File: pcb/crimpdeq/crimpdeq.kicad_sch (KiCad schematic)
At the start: 47 parts, among them J2 USB4105-GF-A, Q1 SS8550, Q2 DMG3415U, U1 ESP32-C3-MINI-1, U2 MCP73831T-2ACI/OT, U3 HX711, U4 Rust_Board, U5 MAX17048G+T10, U6 SY8088

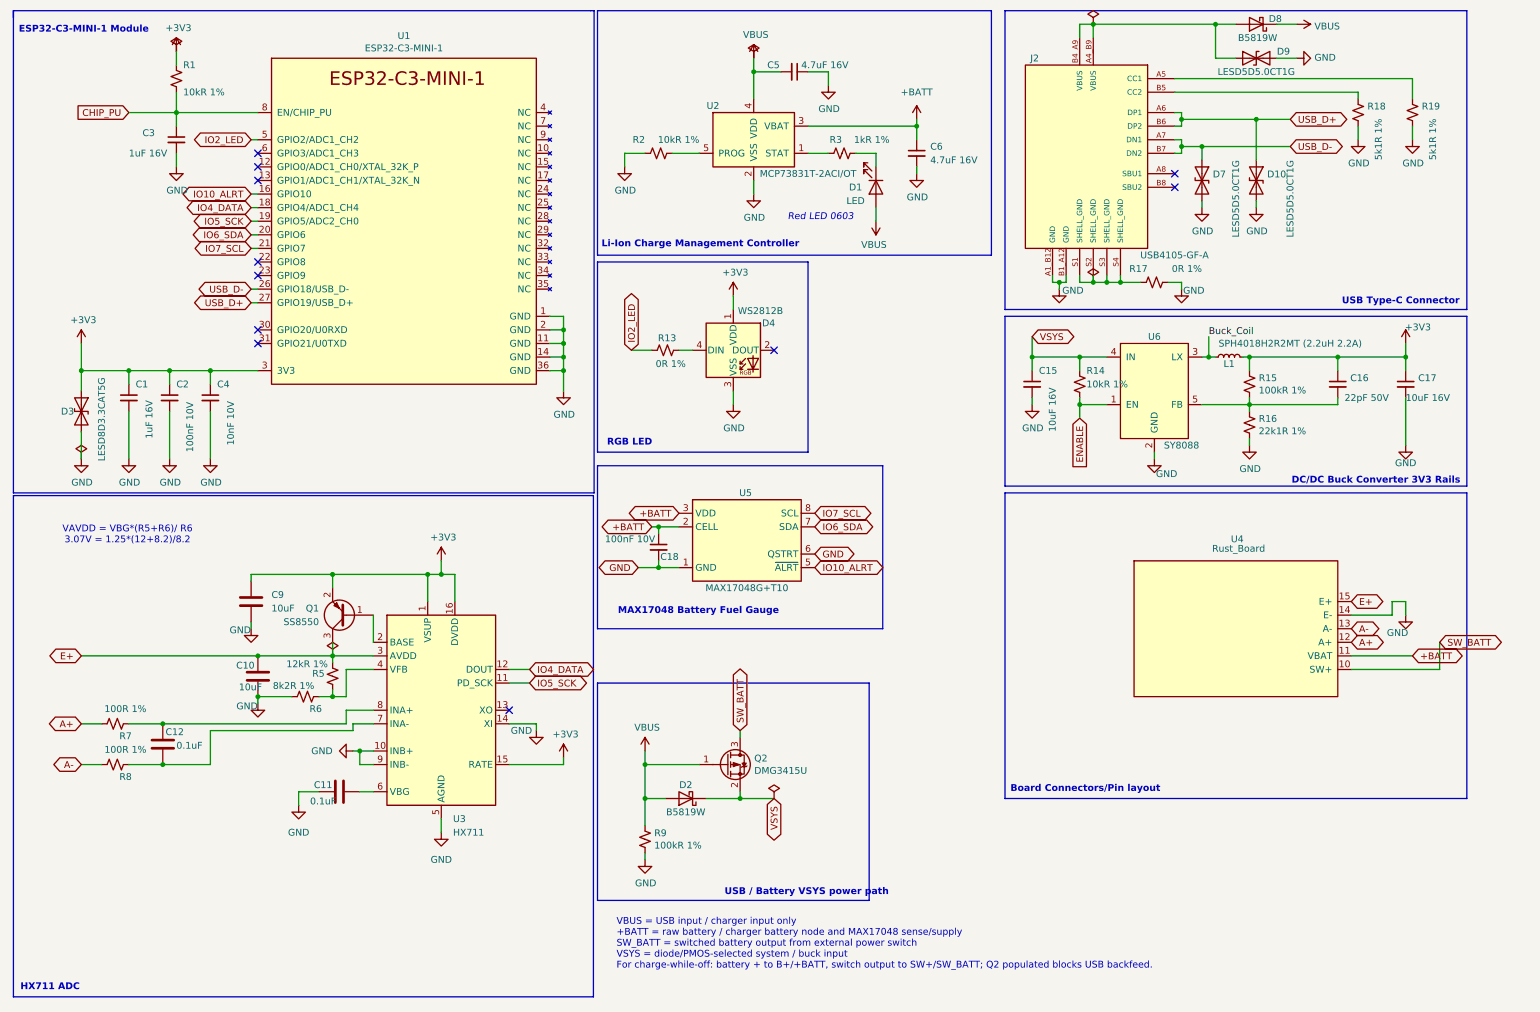
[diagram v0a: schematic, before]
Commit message: Revision 3 (#26)
* Reorganize PCB designs and add crimpdeq-v2-nano (25x26mm 4-layer compact board)

Moves the original design to pcb/designs/crimpdeq-v2/ so each PCB
package can live in its own versioned directory, and adds
pcb/designs/crimpdeq-v2-nano/: a 4-layer, 25 x 26 mm redesign
(~56% smaller board area than crimpdeq-v2: 1467.4 mm2 -> 650.0 mm2)
with the ESP32 antenna and status LED both moved to the back and
USB/HX711 kept on the front.

- Electrically identical to crimpdeq-v2: same 48-component BOM,
  same 197-pad netlist, 0 changed nets
- Passes KiCad DRC (0 violations, 0 unconnected)
- Validated on JLCPCB's website DFM checker: all danger-level
  findings were reviewed and resolved before committing (functional-
  label silk-to-pad/hole clearances, tht-to-smd cable pad gaps,
  USB-C shell slot width). Only conservative warning-level advisories
  remain on the six 1.50 mm cable PTH pads and the USB shell slot
  (see reports/crimpdeq-v2-nano_jlc_tht_to_smd.md)
- Updates the CI matrix to check both designs

Physical prototype validation of antenna performance and connector
fit is still pending.

* Add agents.md and 4-layer/compact reproduction tooling, symlink CLAUDE.md

agents.md documents the frozen BOM/netlist/routing invariants and
session history for the crimpdeq-v2 / crimpdeq-v2-nano designs.
tools/4layer/ and tools/compact/ are the scripted place -> route ->
verify pipeline used to build and DFM-check crimpdeq-v2-nano from
the crimpdeq-v2 baseline. CLAUDE.md is a symlink to agents.md for
AI coding agents that look for that filename by convention.

* fix: prepare nano project for release

* test: lock corrected PCB connectivity

Validate every connected pad against the revised golden netlist so ESP32 ground-pin and pull-up regressions fail immediately.

Co-authored-by: Cursor <cursoragent@cursor.com>

* refactor: consolidate the canonical PCB package

Move shared libraries to the repository root and replace versioned design trees with the corrected prod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
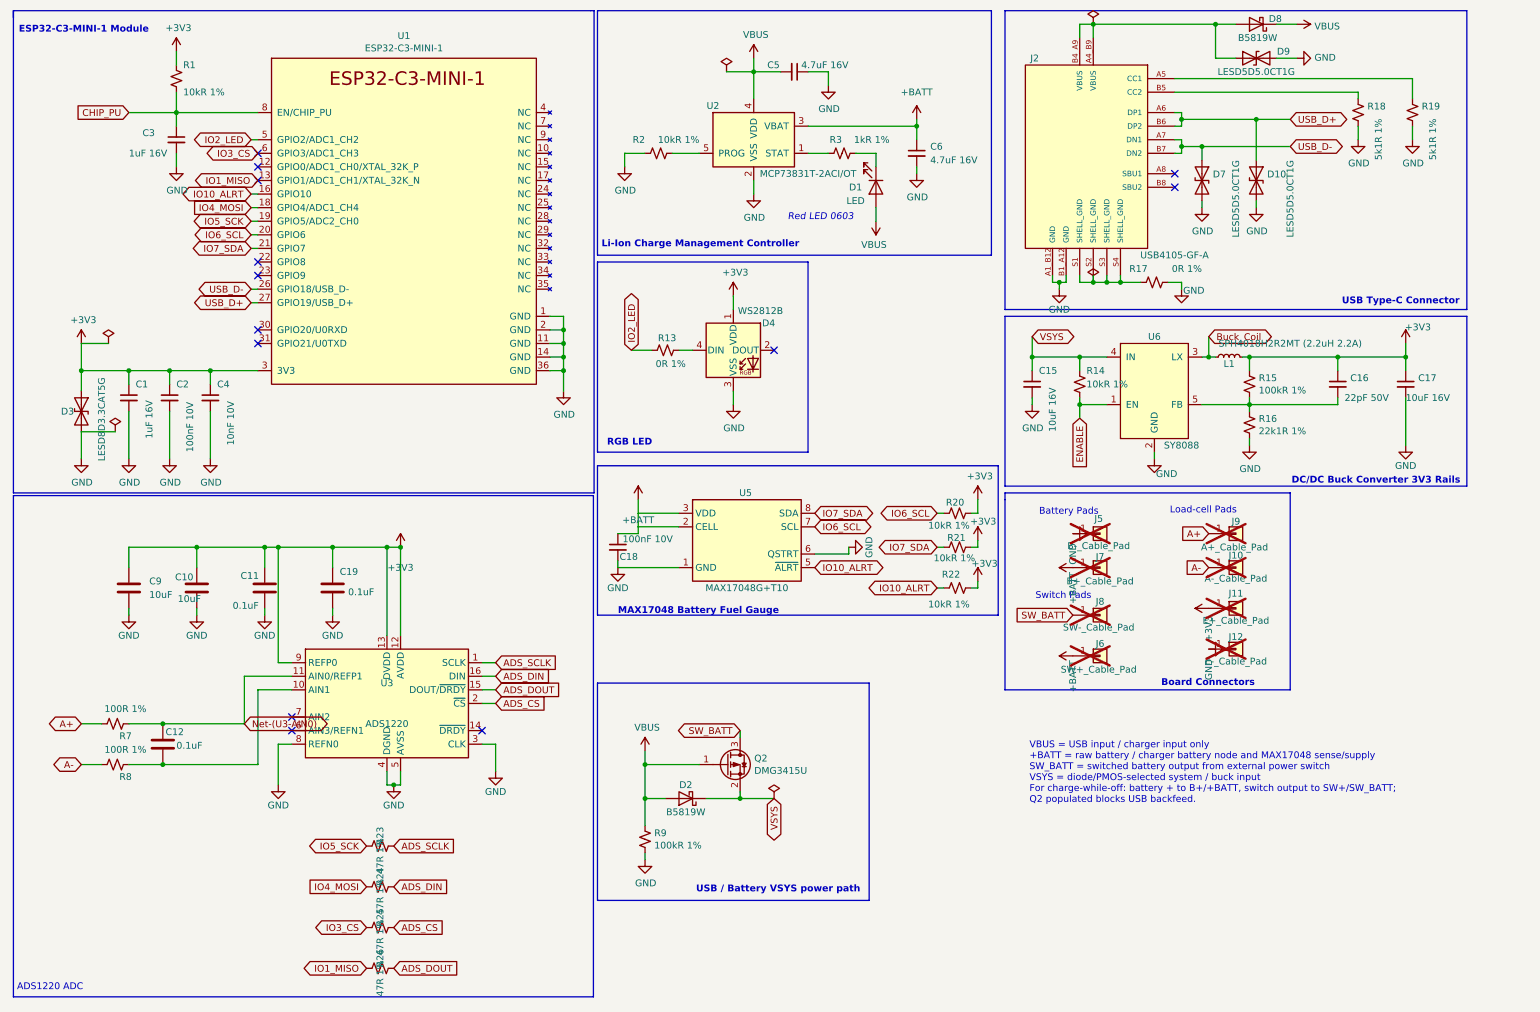
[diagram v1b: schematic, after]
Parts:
- removed Q1: SS8550, Package_TO_SOT_SMD:SOT-23, symbol Transistor_BJT:SS8550
- removed R5: 12kR 1%, Resistor_SMD:R_0402_1005Metric, symbol Device:R_Small_US
- removed R6: 8k2R 1%, Resistor_SMD:R_0402_1005Metric, symbol Device:R_Small_US
- removed U3: HX711, Package_SO:SOP-16_3.9x9.9mm_P1.27mm, symbol Analog_ADC:HX711
- removed U4: Rust_Board, symbol Rust_Board:Rust_Board
- added C19: 0.1uF, Capacitor_SMD:C_0603_1608Metric, symbol Device:C
- added J10: A-_Cable_Pad, TestPoint:TestPoint_THTPad_D1.5mm_Drill0.7mm, symbol Connector_Generic:Conn_01x01
- added J11: E+_Cable_Pad, TestPoint:TestPoint_THTPad_D1.5mm_Drill0.7mm, symbol Connector_Generic:Conn_01x01
- added J12: E-_Cable_Pad, TestPoint:TestPoint_THTPad_D1.5mm_Drill0.7mm, symbol Connector_Generic:Conn_01x01
- added J5: B-_Cable_Pad, TestPoint:TestPoint_THTPad_D1.5mm_Drill0.7mm, symbol Connector_Generic:Conn_01x01
- added J6: SW+_Cable_Pad, TestPoint:TestPoint_THTPad_D1.5mm_Drill0.7mm, symbol Connector_Generic:Conn_01x01
- added J7: B+_Cable_Pad, TestPoint:TestPoint_THTPad_D1.5mm_Drill0.7mm, symbol Connector_Generic:Conn_01x01
- added J8: SW-_Cable_Pad, TestPoint:TestPoint_THTPad_D1.5mm_Drill0.7mm, symbol Connector_Generic:Conn_01x01
- added J9: A+_Cable_Pad, TestPoint:TestPoint_THTPad_D1.5mm_Drill0.7mm, symbol Connector_Generic:Conn_01x01
- added R20, R21, R22: 10kR 1%, Resistor_SMD:R_0402_1005Metric, symbol Device:R_Small_US
- added R23, R24, R25, R26: 47R 1%, Resistor_SMD:R_0402_1005Metric, symbol Device:R_Small_US
- added U3: ADS1220, Package_SO:TSSOP-16_4.4x5mm_P0.65mm, symbol Analog_ADC:ADS1220xPW
- C12: footprint Capacitor_SMD:C_0603_1608Metric -> Capacitor_SMD:C_1206_3216Metric; LCSC (none) -> C405303; MPN (none) -> GRM31C5C2A104JA01L; Manufacturer (none) -> Murata
- D4: LCSC (none) -> C52917433; MANUFACTURER (none) -> Worldsemi; MPN (none) -> WS2812B-V6
- J2: footprint Rust_Board:GCT_USB4105-GF-A -> Crimpdeq:GCT_USB4105-GF-A; symbol Rust_Board:USB4105-GF-A -> Crimpdeq:USB4105-GF-A; MPN (none) -> USB4105-GF-A
- Q2: footprint Package_TO_SOT_SMD:SOT-23 -> Crimpdeq:SOT-23; symbol Transistor_FET:DMG2301L -> Transistor_FET:Q_PMOS_GSD; MANUFACTURER (none) -> Diodes Incorporated; MPN (none) -> DMG3415U-7
- R7, R8: LCSC C25741 -> C25076
- U1: footprint PCM_Espressif:ESP32-C3-MINI-1 -> Crimpdeq:ESP32-C3-MINI-1; symbol Espressif:ESP32-C3-MINI-1 -> Crimpdeq:ESP32-C3-MINI-1; MANUFACTURER (none) -> Espressif Systems; MPN (none) -> ESP32-C3-MINI-1
- U2: footprint Package_TO_SOT_SMD:SOT-23-5 -> Crimpdeq:MCP73831_SOT-23-5
- U5: symbol Battery_Management:MAX17048 -> Crimpdeq:MAX17048; LCSC (none) -> C2682616; MANUFACTURER (none) -> Analog Devices / Maxim Integrated; MPN (none) -> MAX17048G+T10
- U6: footprint Package_TO_SOT_SMD:SOT-23-5 -> Crimpdeq:SY8088_SOT-23-5; symbol Rust_Board:SY8088 -> Crimpdeq:SY8088
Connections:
- net E+ is gone; now on net +3V3: C10.1
- net +3V3: now also C11.1, C19.1, J11.1 (Pin_1), R20.2, R21.2, R22.2, U3.12 (AVDD), U3.13 (DVDD), U3.9 (REFP0)
- net +BATT: now also J6.1 (Pin_1), J7.1 (Pin_1)
- net A+: now also J9.1 (Pin_1)
- net A-: now also J10.1 (Pin_1)
- net GND: now also C11.2, U1.37 (GND), U1.38 (GND), U1.39 (GND), U1.40 (GND), U1.41 (GND), U1.42 (GND), U1.43 (GND), U1.44 (GND), U1.45 (GND), U1.46 (GND), U1.47 (GND), U1.48 (GND), U1.49 (GND), U1.50 (GND), U1.51 (GND), U1.52 (GND), U1.53 (GND), C19.2, J12.1 (Pin_1), J5.1 (Pin_1), U3.3 (CLK), U3.4 (DGND), U3.5 (AVSS), U3.8 (REFN0); no longer C11.1
- net IO10_ALRT: now also R22.1
- net IO5_SCK: now also R23.1
- net SW_BATT: now also J8.1 (Pin_1)
- net Net-(U3-AIN0): now reaches C12.1, R7.1
- net Net-(U3-AIN0): now also U3.11 (AIN0/REFP1)
- net at C12.2, R8.1: now also U3.10 (AIN1)
- net IO1_MISO: now reaches U1.13 (GPIO1/ADC1_CH1/XTAL_32K_N)
- net IO1_MISO: now also R26.2
- net IO3_CS: now reaches U1.6 (GPIO3/ADC1_CH3)
- net IO3_CS: now also R25.1
- net IO4_DATA renamed IO4_MOSI
- net IO4_MOSI: now also R24.1
- net IO6_SDA renamed IO6_SCL
- net IO6_SCL: now also R20.1
- net IO7_SCL renamed IO7_SDA
- net IO7_SDA: now also R21.1
- new net ADS_CS: R25.2, U3.2 (~{CS})
- new net ADS_DIN: R24.2, U3.16 (DIN)
- new net ADS_DOUT: R26.1, U3.15 (DOUT/~{DRDY})
- new net ADS_SCLK: R23.2, U3.1 (SCLK)
- no-connect marks 11 -> 13
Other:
- note added: "ADS1220 ADC"
- note added: "Battery Pads"
- note added: "Board Connectors"
- note added: "Load-cell Pads"
- note added: "Switch Pads"
- note removed: "Board Connectors/Pin layout"
- note removed: "HX711 ADC"
- note removed: "VAVDD = VBG*(R5+R6)/ R6 3.07V = 1.25*(12+8.2)/8.2"
- moved on the sheet: C10, C18, C9
